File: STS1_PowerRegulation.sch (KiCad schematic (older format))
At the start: 25 parts, among them U2 LT3120

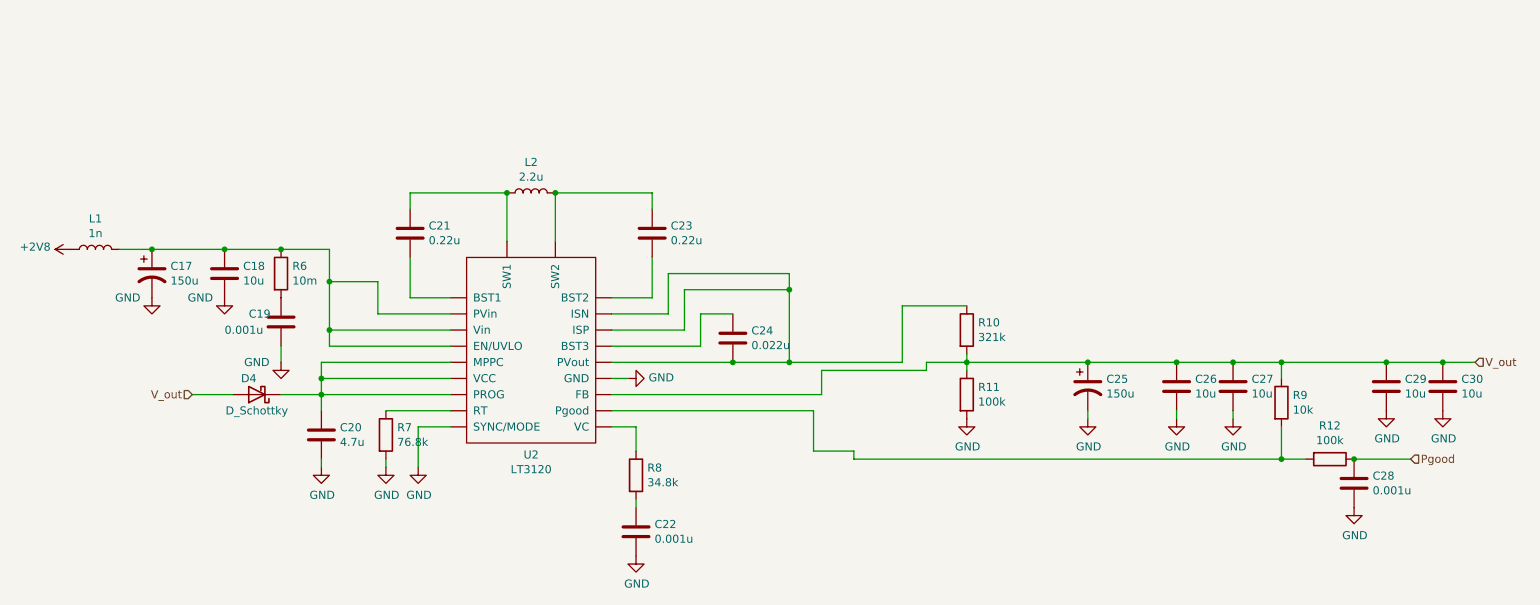
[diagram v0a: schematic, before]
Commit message: Add basic schematic for 5V DCDC
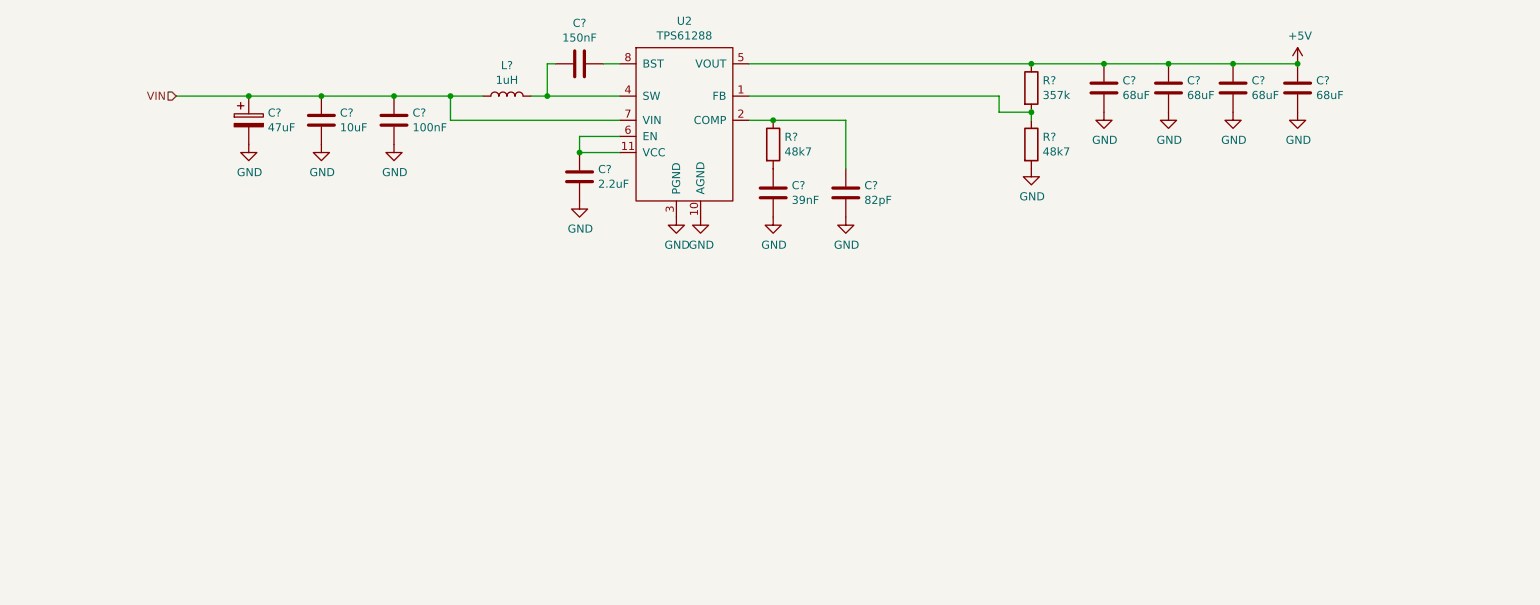
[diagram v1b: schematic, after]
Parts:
- removed C17, C25: 150u, symbol Device:CP1
- removed C18, C26, C27, C29, C30: 10u, symbol Device:C
- removed C19, C22, C28: 0.001u, symbol Device:C
- removed C20: 4.7u, symbol Device:C
- removed C21, C23: 0.22u, symbol Device:C
- removed C24: 0.022u, symbol Device:C
- removed D4: D_Schottky, symbol Device:D_Schottky
- removed L1: 1n, symbol Device:L
- removed L2: 2.2u, symbol Device:L
- removed R10: 321k, symbol Device:R
- removed R11, R12: 100k, symbol Device:R
- removed R6: 10m, symbol Device:R
- removed R7: 76.8k, symbol Device:R
- removed R8: 34.8k, symbol Device:R
- removed R9: 10k, symbol Device:R
- removed U2: LT3120, symbol STS1BuckBoost:LT3120
- added C?: 2.2uF, symbol Device:C
- added C?: 150nF, symbol Device:C
- added C?: 100nF, symbol Device:C
- added C?: 10uF, symbol Device:C
- added C?: 47uF, symbol Device:CP
- added C?: 39nF, symbol Device:C
- added C?: 82pF, symbol Device:C
- added C? (x4): 68uF, symbol Device:C
- added L?: 1uH, symbol Device:L
- added R?: 357k, symbol Device:R
- added R? (x2): 48k7, symbol Device:R
- added U2: TPS61288, STS1_DCDC:VQFN-HR, symbol STS1_DCDC:TPS61288
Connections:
- net GND: now also C?.2, C?.2, C?.2, C?.2, C?.2, C?.2, C?.2, C?.2, C?.2, C?.2, R?.2, U2.10 (AGND), U2.3 (PGND)
- new net: R?.1, R?.2, U2.1 (FB)
- new net: C?.1, U2.11 (VCC), U2.6 (EN)
- new net: C?.1, R?.1, U2.2 (COMP)
- new net: C?.2, L?.2, U2.4 (SW), U2.9 (SW)
- new net: C?.1, U2.8 (BST)
- new net: C?.1, R?.2
- new net +5V: C?.1, C?.1, C?.1, C?.1, R?.1, U2.5 (VOUT)
- new net VIN: C?.1, C?.1, C?.1, L?.1, U2.7 (VIN)
